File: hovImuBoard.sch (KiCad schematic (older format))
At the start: 77 parts, among them J1 AVR-ISP-6, J2 Ext. Power, J3 54602-908LF, J4 AVR-JTAG-10, J5 ExtensionPort, U1 LD2981, U2 BMX160, U3 SN65HVD32DR, U4 ATmega1284P-AU, U5 TPS62173DSG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

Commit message: First shot routing the board
Simplified the design: The IP address is not configurable with solder jumpers any more.
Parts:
- removed JP1: J15, Jumper:SolderJumper-2_P1.3mm_Bridged_Pad1.0x1.5mm, symbol Jumper:SolderJumper_2_Bridged
- removed JP10: J6, Jumper:SolderJumper-2_P1.3mm_Open_Pad1.0x1.5mm, symbol Jumper:SolderJumper_2_Open
- removed JP11: J5, Jumper:SolderJumper-2_P1.3mm_Open_Pad1.0x1.5mm, symbol Jumper:SolderJumper_2_Open
- removed JP12: J4, Jumper:SolderJumper-2_P1.3mm_Open_Pad1.0x1.5mm, symbol Jumper:SolderJumper_2_Open
- removed JP13: J3, Jumper:SolderJumper-2_P1.3mm_Open_Pad1.0x1.5mm, symbol Jumper:SolderJumper_2_Open
- removed JP14: J2, Jumper:SolderJumper-2_P1.3mm_Open_Pad1.0x1.5mm, symbol Jumper:SolderJumper_2_Open
- removed JP15: J1, Jumper:SolderJumper-2_P1.3mm_Bridged_Pad1.0x1.5mm, symbol Jumper:SolderJumper_2_Bridged
- removed JP16: J0, Jumper:SolderJumper-2_P1.3mm_Open_Pad1.0x1.5mm, symbol Jumper:SolderJumper_2_Open
- removed JP2: J14, Jumper:SolderJumper-2_P1.3mm_Bridged_Pad1.0x1.5mm, symbol Jumper:SolderJumper_2_Bridged
- removed JP3: J13, Jumper:SolderJumper-2_P1.3mm_Open_Pad1.0x1.5mm, symbol Jumper:SolderJumper_2_Open
- removed JP4: J12, Jumper:SolderJumper-2_P1.3mm_Open_Pad1.0x1.5mm, symbol Jumper:SolderJumper_2_Open
- removed JP5: J11, Jumper:SolderJumper-2_P1.3mm_Bridged_Pad1.0x1.5mm, symbol Jumper:SolderJumper_2_Bridged
- removed JP6: J10, Jumper:SolderJumper-2_P1.3mm_Bridged_Pad1.0x1.5mm, symbol Jumper:SolderJumper_2_Bridged
- removed JP7: J9, Jumper:SolderJumper-2_P1.3mm_Bridged_Pad1.0x1.5mm, symbol Jumper:SolderJumper_2_Bridged
- removed JP8: J8, Jumper:SolderJumper-2_P1.3mm_Bridged_Pad1.0x1.5mm, symbol Jumper:SolderJumper_2_Bridged
- removed JP9: J7, Jumper:SolderJumper-2_P1.3mm_Open_Pad1.0x1.5mm, symbol Jumper:SolderJumper_2_Open
- removed RN1, RN2: 470K x 8, Resistor_THT:R_Array_SIP9, symbol Device:R_Network08
- added TP1: +3.3V_IMU, TestPoint:TestPoint_THTPad_D1.0mm_Drill0.5mm, symbol Connector:TestPoint
- added TP2: +12V, TestPoint:TestPoint_THTPad_D1.0mm_Drill0.5mm, symbol Connector:TestPoint
- added TP3: +5V, TestPoint:TestPoint_THTPad_D1.0mm_Drill0.5mm, symbol Connector:TestPoint
- added TP4: +3.3V, TestPoint:TestPoint_THTPad_D1.0mm_Drill0.5mm, symbol Connector:TestPoint
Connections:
- net labels removed: IP0, IP1, IP10, IP11, IP12, IP13, IP14, IP15, IP2, IP3, IP4, IP5, IP6, IP7, IP8, IP9, IP[0..15]
- wire segments 254 -> 187
- no-connect marks 9 -> 25
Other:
- note removed: "."
- note removed: "192.168.203."
- note removed: "2"
- note removed: "Local IP Address encoding. Default 192.168.203.2"

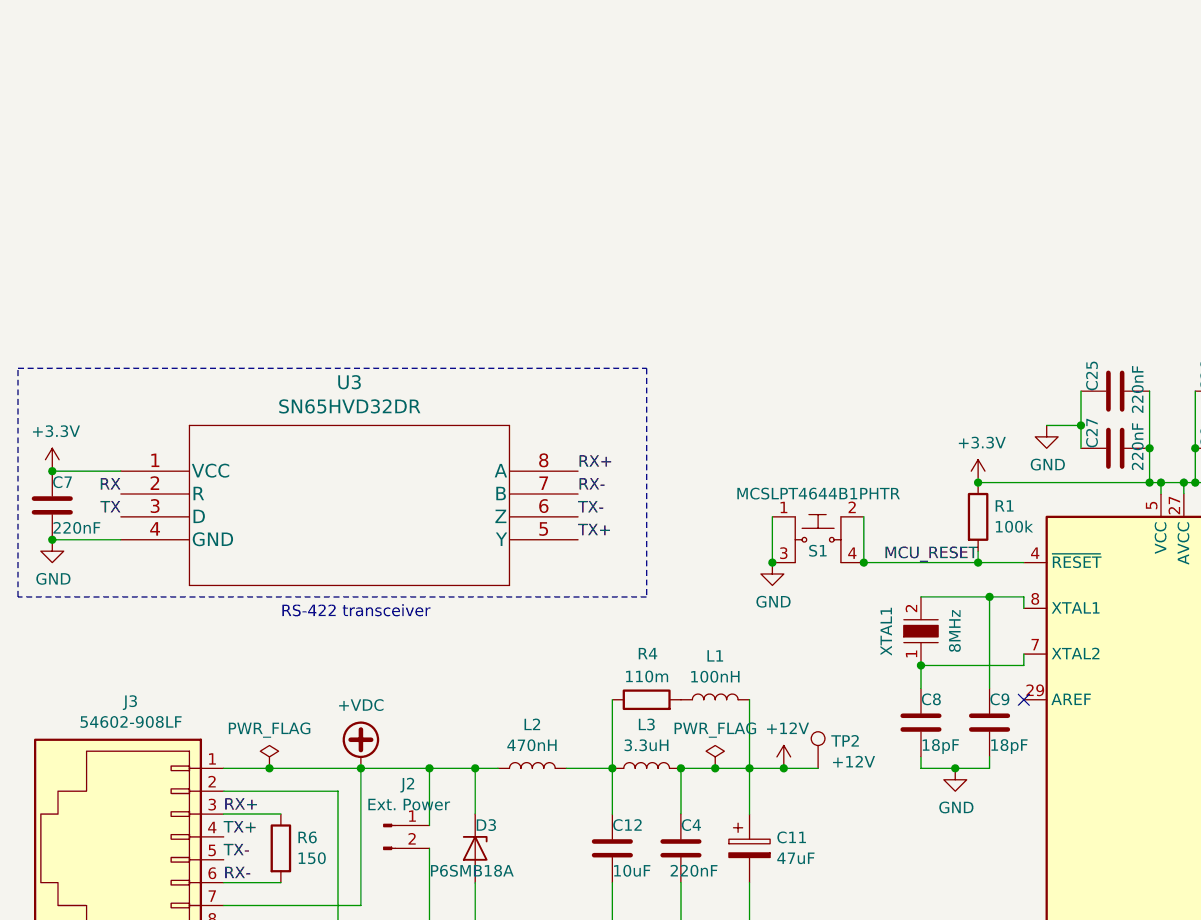
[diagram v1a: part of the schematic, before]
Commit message: Re-arrange expansion port and LEDs. Route power further apart from the BMX160 Add mounting holes.
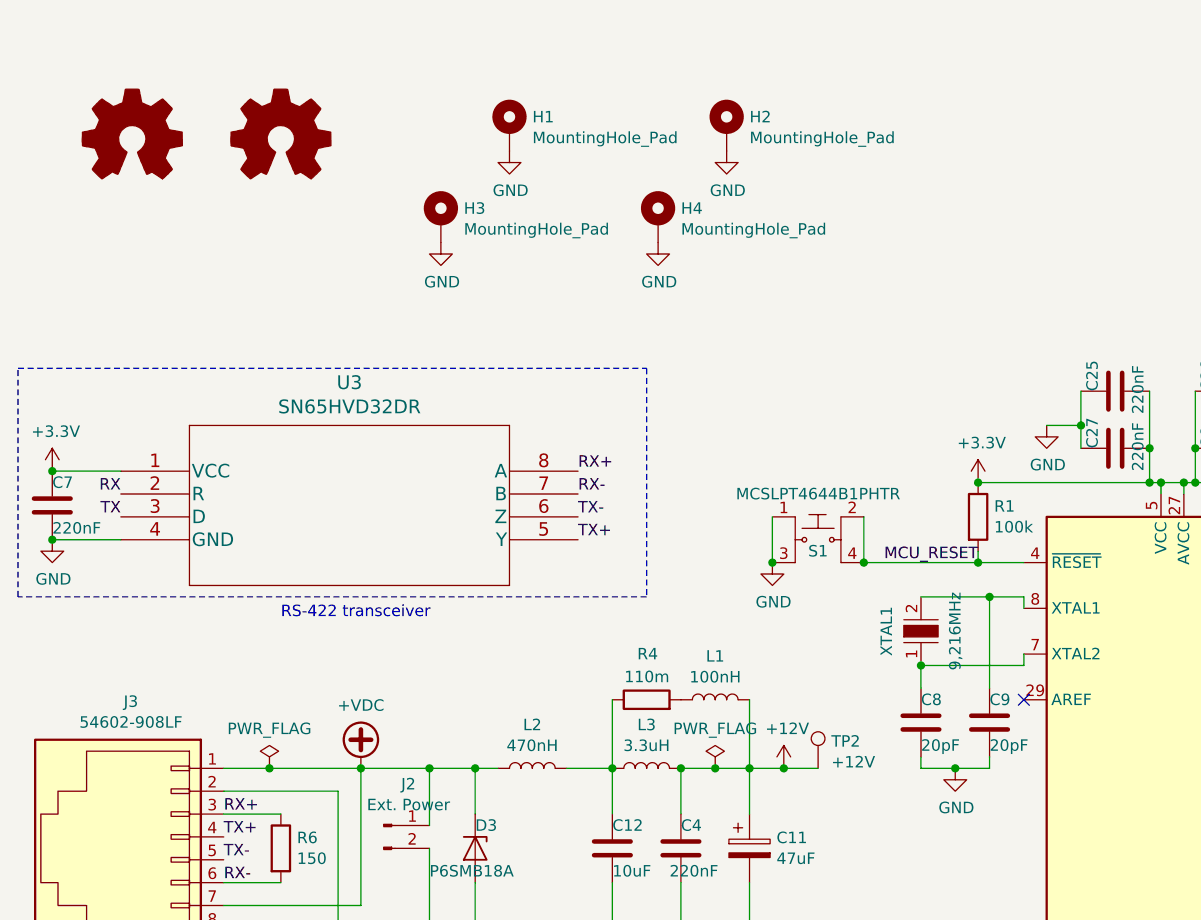
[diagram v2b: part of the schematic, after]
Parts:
- added H1, H2, H3, H4: MountingHole_Pad, MountingHole:MountingHole_2.7mm_M2.5_Pad_Via, symbol Mechanical:MountingHole_Pad
- added LOGO1, LOGO2: Logo_Open_Hardware_Small, Symbol:OSHW-Symbol_6.7x6mm_Copper, symbol Graphic:Logo_Open_Hardware_Small
- C8, C9: value 18pF -> 20pF; Digi-Key_PN 1276-1107-1-ND -> 1276-1829-1-ND; MPN CL21C180JBANNNC -> CL21C200JBANNNC
- XTAL1: value 8MHz -> 9,216MHz; Category Crystals, Oscillators, Resonators -> (none); Description 8MHz ±30ppm Crystal 18pF 80 Ohms HC-49/US -> (none); Digi-Key_PN 535-9864-1-ND -> XC1274CT-ND; Family Crystals -> (none); MPN ABLS2-8.000MHZ-D4Y-T -> ECS-92.1-20-5PX-TR; Manufacturer Abracon LLC -> ECS Inc.; Status Active -> (none)
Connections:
- net GND: now also H1.1, H2.1, H3.1, H4.1
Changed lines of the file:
@@
 P 5150 3550
 F 0 "C8" H 5150 3450 50  0000 R CNN
-F 1 "18pF" H 5150 3650 50  0000 R CNN
+F 1 "20pF" H 5150 3650 50  0000 R CNN
 F 2 "Capacitor_SMD:C_0805_2012Metric" H 5188 3400 50  0001 C CNN
-F 3 "http://www.samsungsem.com/kr/support/product-search/mlcc/CL21C180JBANNNC.jsp" H 5150 3550 50  0001 C CNN
-F 4 "1276-1107-1-ND" V 5150 3550 50  0001 C CNN "Digi-Key_PN"
-F 5 "CL21C180JBANNNC" V 5150 3550 50  0001 C CNN "MPN"
+F 3 "http://www.samsungsem.com/kr/support/product-search/mlcc/CL21C200JBANNNC.jsp" H 5150 3550 50  0001 C CNN
+F 4 "1276-1829-1-ND" V 5150 3550 50  0001 C CNN "Digi-Key_PN"
+F 5 "CL21C200JBANNNC" V 5150 3550 50  0001 C CNN "MPN"
 F 6 "Samsung Electro-Mechanics" V 5150 3550 50  0001 C CNN "Manufacturer"
 	1    5150 3550
-	-1   0    0    1
-$EndComp
-$Comp
-L Device:C C9
-U 1 1 5D5248EF
-P 5450 3550
-F 0 "C9" H 5450 3450 50  0000 R CNN
-F 1 "18pF" H 5450 3650 50  0000 R CNN
-F 2 "Capacitor_SMD:C_0805_2012Metric" H 5488 3400 50  0001 C CNN
-F 3 "http://www.samsungsem.com/kr/support/product-search/mlcc/CL21C180JBANNNC.jsp" H 5450 3550 50  0001 C CNN
-F 4 "1276-1107-1-ND" V 5450 3550 50  0001 C CNN "Digi-Key_PN"
-F 5 "CL21C180JBANNNC" V 5450 3550 50  0001 C CNN "MPN"
-F 6 "Samsung Electro-Mechanics" V 5450 3550 50  0001 C CNN "Manufacturer"
-	1    5450 3550
 	-1   0    0    1
 $EndComp
@@
 P 5150 3150
 F 0 "XTAL1" H 5150 3300 50  0000 C CNN
-F 1 "8MHz" H 5150 3000 50  0000 C CNN
+F 1 "9,216MHz" H 5150 3000 50  0000 C CNN
 F 2 "Crystal:Crystal_SMD_HC49-SD" H 5350 3350 60  0001 L CNN
-F 3 "https://abracon.com/Resonators/ABLS2.pdf" H 5350 3450 60  0001 L CNN
-F 4 "535-9864-1-ND" H 5350 3550 60  0001 L CNN "Digi-Key_PN"
-F 5 "ABLS2-8.000MHZ-D4Y-T" H 5350 3650 60  0001 L CNN "MPN"
-F 6 "Crystals, Oscillators, Resonators" H 5350 3750 60  0001 L CNN "Category"
-F 7 "Crystals" H 5350 3850 60  0001 L CNN "Family"
-F 8 "8MHz ±30ppm Crystal 18pF 80 Ohms HC-49/US" H 5350 4150 60  0001 L CNN "Description"
-F 9 "Abracon LLC" H 5350 4250 60  0001 L CNN "Manufacturer"
-F 10 "Active" H 5350 4350 60  0001 L CNN "Status"
+F 3 "https://www.ecsxtal.com/store/pdf/csm-7x.pdf" H 5350 3450 60  0001 L CNN
+F 4 "XC1274CT-ND" H 5350 3550 60  0001 L CNN "Digi-Key_PN"
+F 5 "ECS-92.1-20-5PX-TR" H 5350 3650 60  0001 L CNN "MPN"
+F 6 "ECS Inc." H 5350 4250 60  0001 L CNN "Manufacturer"
 	1    5150 3150
 	0    -1   -1   0
@@
 NoConn ~ 6800 6150
 NoConn ~ 6800 6250
+$Comp
+L Device:C C9
+U 1 1 5D5F3117
+P 5450 3550
+F 0 "C9" H 5450 3450 50  0000 R CNN
+F 1 "20pF" H 5450 3650 50  0000 R CNN
+F 2 "Capacitor_SMD:C_0805_2012Metric" H 5488 3400 50  0001 C CNN
+F 3 "http://www.samsungsem.com/kr/support/product-search/mlcc/CL21C200JBANNNC.jsp" H 5450 3550 50  0001 C CNN
+F 4 "1276-1829-1-ND" V 5450 3550 50  0001 C CNN "Digi-Key_PN"
+F 5 "CL21C200JBANNNC" V 5450 3550 50  0001 C CNN "MPN"
+F 6 "Samsung Electro-Mechanics" V 5450 3550 50  0001 C CNN "Manufacturer"
+	1    5450 3550
+	-1   0    0    1
+$EndComp
+$Comp
+L Graphic:Logo_Open_Hardware_Small LOGO1
+U 1 1 5D5F614B
+P 1700 1000
+F 0 "LOGO1" H 1700 1275 50  0001 C CNN
+F 1 "Logo_Open_Hardware_Small" H 1700 775 50  0001 C CNN
+F 2 "Symbol:OSHW-Symbol_6.7x6mm_Copper" H 1700 1000 50  0001 C CNN
+F 3 "~" H 1700 1000 50  0001 C CNN
+	1    1700 1000
+	1    0    0    -1
+$EndComp
+$Comp
+L Graphic:Logo_Open_Hardware_Small LOGO2
+U 1 1 5D5F6CFD
+P 2350 1000
+F 0 "LOGO2" H 2350 1275 50  0001 C CNN
+F 1 "Logo_Open_Hardware_Small" H 2350 775 50  0001 C CNN
+F 2 "Symbol:OSHW-Symbol_6.7x6mm_Copper" H 2350 1000 50  0001 C CNN
+F 3 "~" H 2350 1000 50  0001 C CNN
+	1    2350 1000
+	1    0    0    -1
+$EndComp
+$Comp
+L Mechanical:MountingHole_Pad H1
+U 1 1 5D5F84F4
+P 3350 950
+F 0 "H1" H 3450 999 50  0000 L CNN
+F 1 "MountingHole_Pad" H 3450 908 50  0000 L CNN
+F 2 "MountingHole:MountingHole_2.7mm_M2.5_Pad_Via" H 3350 950 50  0001 C CNN
+F 3 "~" H 3350 950 50  0001 C CNN
+	1    3350 950
+	1    0    0    -1
+$EndComp
+$Comp
+L Mechanical:MountingHole_Pad H3
+U 1 1 5D5FB788
+P 3050 1350
+F 0 "H3" H 3150 1399 50  0000 L CNN
+F 1 "MountingHole_Pad" H 3150 1308 50  0000 L CNN
+F 2 "MountingHole:MountingHole_2.7mm_M2.5_Pad_Via" H 3050 1350 50  0001 C CNN
+F 3 "~" H 3050 1350 50  0001 C CNN
+	1    3050 1350
+	1    0    0    -1
+$EndComp
+$Comp
+L Mechanical:MountingHole_Pad H2
+U 1 1 5D5FB92A
+P 4300 950
+F 0 "H2" H 4400 999 50  0000 L CNN
+F 1 "MountingHole_Pad" H 4400 908 50  0000 L CNN
+F 2 "MountingHole:MountingHole_2.7mm_M2.5_Pad_Via" H 4300 950 50  0001 C CNN
+F 3 "~" H 4300 950 50  0001 C CNN
+	1    4300 950
+	1    0    0    -1
+$EndComp
+$Comp
+L Mechanical:MountingHole_Pad H4
+U 1 1 5D5FC33E
+P 4000 1350
+F 0 "H4" H 4100 1399 50  0000 L CNN
+F 1 "MountingHole_Pad" H 4100 1308 50  0000 L CNN
+F 2 "MountingHole:MountingHole_2.7mm_M2.5_Pad_Via" H 4000 1350 50  0001 C CNN
+F 3 "~" H 4000 1350 50  0001 C CNN
+	1    4000 1350
+	1    0    0    -1
+$EndComp
+$Comp
+L power:GND #PWR?
+U 1 1 5D6733FB
+P 3050 1450
+F 0 "#PWR?" H 3050 1200 50  0001 C CNN
+F 1 "GND" H 3055 1277 50  0000 C CNN
+F 2 "" H 3050 1450 50  0001 C CNN
+F 3 "" H 3050 1450 50  0001 C CNN
+	1    3050 1450
+	1    0    0    -1
+$EndComp
+$Comp
+L power:GND #PWR?
+U 1 1 5D673B74
+P 4000 1450
+F 0 "#PWR?" H 4000 1200 50  0001 C CNN
+F 1 "GND" H 4005 1277 50  0000 C CNN
+F 2 "" H 4000 1450 50  0001 C CNN
+F 3 "" H 4000 1450 50  0001 C CNN
+	1    4000 1450
+	1    0    0    -1
+$EndComp
+$Comp
+L power:GND #PWR?
+U 1 1 5D673E04
+P 4300 1050
+F 0 "#PWR?" H 4300 800 50  0001 C CNN
+F 1 "GND" H 4305 877 50  0000 C CNN
+F 2 "" H 4300 1050 50  0001 C CNN
+F 3 "" H 4300 1050 50  0001 C CNN
+	1    4300 1050
+	1    0    0    -1
+$EndComp
+$Comp
+L power:GND #PWR?
+U 1 1 5D673E67
+P 3350 1050
+F 0 "#PWR?" H 3350 800 50  0001 C CNN
+F 1 "GND" H 3355 877 50  0000 C CNN
+F 2 "" H 3350 1050 50  0001 C CNN
+F 3 "" H 3350 1050 50  0001 C CNN
+	1    3350 1050
+	1    0    0    -1
+$EndComp
 $EndSCHEMATC
